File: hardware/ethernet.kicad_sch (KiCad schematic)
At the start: 32 parts, among them J2 DGUK411Q211DB2A1DP2, U2 W5500, X2 25MHz

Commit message: hardware: 4-layer board, placement on both sides, J1 dimensioned
Takes the PCB from bare footprints to a fully placed 4-layer board. No
copper is routed yet and no zones are poured.

Stackup and outline
  Two inner copper layers added: In1.Cu intended as a solid ground plane
  directly beneath the component side, In2.Cu for power distribution. The
  board stays 62 x 68 mm. It is deliberately NOT grown: depth adds mass and
  lengthens the moment arm from the RJ45 cable back to the GPIB connector,
  and the mechanical load path is the connector's two M3 jackscrews on
  46.8 mm centres rather than its 24 signal contacts.

Placement
  All 90 footprints placed: 19 on F.Cu, 71 on B.Cu. Assembly is by hand, so
  back-side passives cost nothing and the 3D-printed enclosure accommodates
  them. Each decoupling capacitor sits on B.Cu directly beneath its IC's
  supply pin, so the connection is a through-via rather than a trace - the
  tightest supply loop available, and it costs no front-side area. That is
  what let the board stay 62 x 68 at ~35% front-side courtyard utilisation
  instead of the 68.7% a single-sided layout needed.

  Verified: zero courtyard overlaps; crystal load caps 0.00-4.00 mm from
  their crystals; C_U3a1 and C_U4a1 at 0.00 mm from their transceivers.

  Done with KiCad's own Flip() transform via the pcbnew Python API, one
  atomic pass, so pads, silkscreen, courtyards and 3D model offsets all
  moved correctly. auto_place_from_schematic was tried and rejected: it
  scored 15 -> 0, planned two parts to identical coordinates and put one
  off-board.

J1 GPIB connector
  Rotated 180 so the pad rows sit at the front edge and the shroud
  overhangs off-board, instead of the body consuming 24 mm of board depth.
  Set back so the two M3 mounting holes are 10.70 mm from the front edge
  per the mechanical drawing; hole span measures 46.80 mm, matching the
  datasheet. This costs 7.84 mm of board depth versus the earlier position
  and reduces the overhang to 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
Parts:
- C_1V2O1, C_BIAS1, C_ETHa1, C_ETHb1, C_ETHbulk1, C_ETHc1, C_ETHd1, C_RCT1, C_TCT1, C_TOCAP1, C_VDD1, C_X2a1, C_X2b1: footprint (none) -> Capacitor_SMD:C_0805_2012Metric
- L2: footprint (none) -> Inductor_SMD:L_0603_1608Metric
- RSET1, R_B1, R_INTP1, R_LEDL1, R_LEDR1, R_RSTP1, R_RX1, R_RX2, R_T1, R_T2, R_T3, R_T4, R_TX1, R_TX2, R_XF1: footprint (none) -> Resistor_SMD:R_0805_2012Metric
- X2: footprint (none) -> Crystal:Crystal_SMD_3225-4Pin_3.2x2.5mm
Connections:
- net GND: now also J2.S1, J2.S2

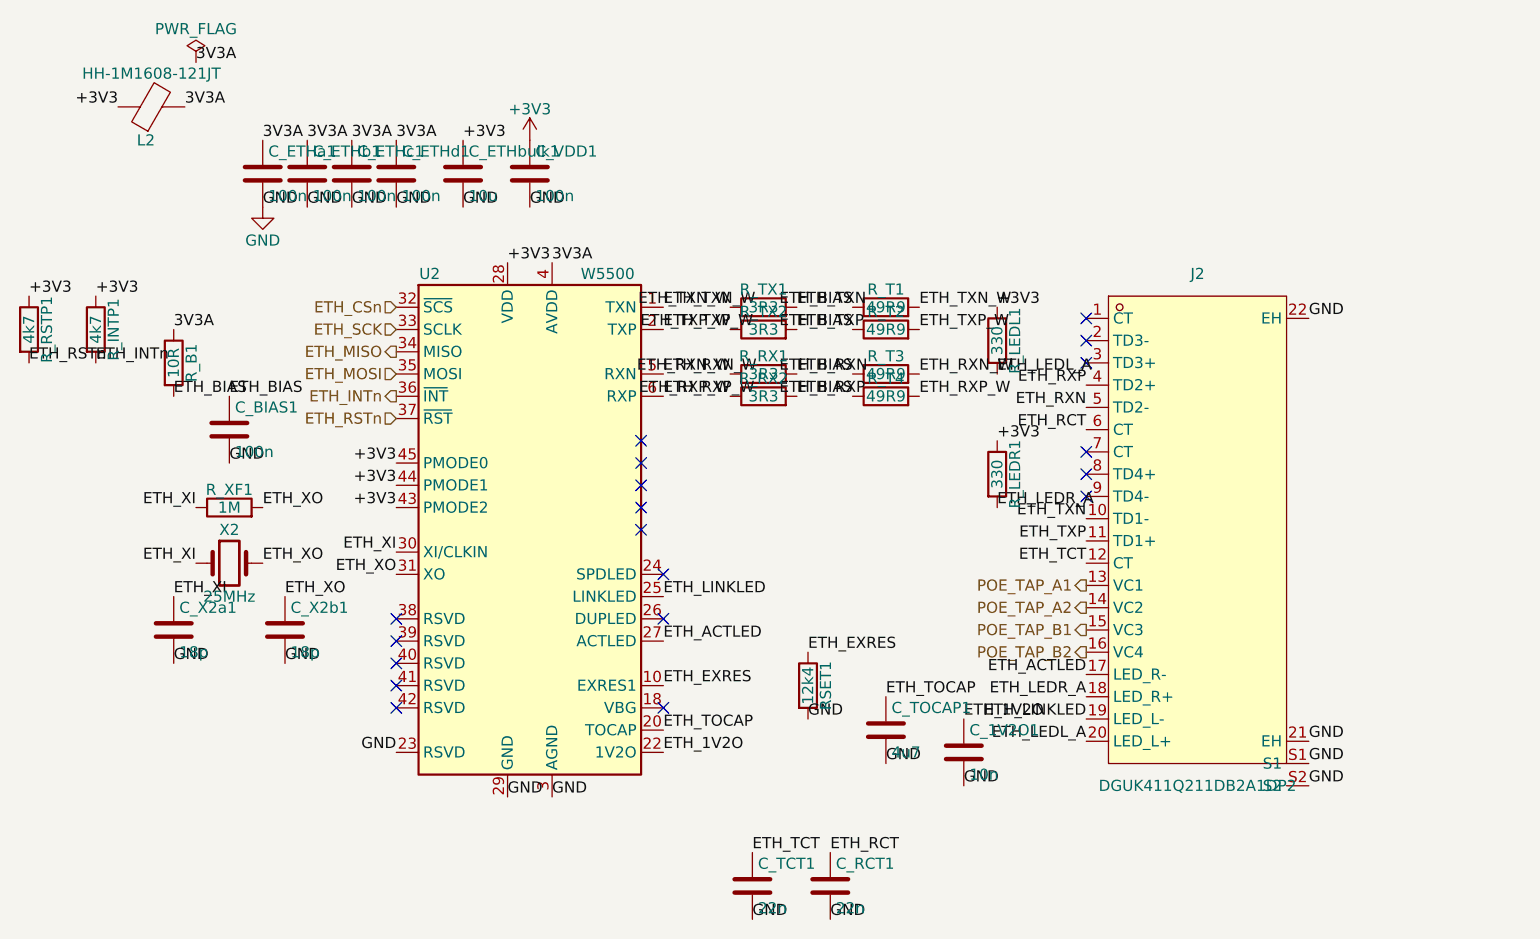
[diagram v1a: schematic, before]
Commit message: hardware: USB-C alternate power source, J2 swapped to HanRun HR871150C
Implements the USB-C-as-alternative-power-source design (design-spec
§30.1): a 1x3 2.54mm header (J4) selects the system rail source via a
jumper rather than a diode-OR, since a Schottky drop would put +5V_SYS
below the SN75160B/161B's 4.75V minimum. Pin 1 = +5V_POE (M1's isolated
output), pin 2 = +5V_SYS (everything downstream), pin 3 = VBUS (from
J3's USB-C pads, already present with 5k1 CC pull-downs). R_G1/C_G1 stay
referenced to +5V_SYS along with Q1's source (R-HW-020): the gate
pull-up must track whichever rail the source actually sits on, or Q1
turns on with IOVDD absent whenever the other source is unpowered.

J2 (PoE RJ45) swapped from a generic MagJack footprint to the actual
ordered part, HanRun HR871150C (LCSC C19724786), correcting the PoE tap
pin numbers (J2.7-10, was J2.13-16) and the shield/ground pin scheme
against its real datasheet pinout.

Added docs/rp2354a-pinmap.md (RP2354A pin assignments) and
hardware/adapter.kicad_dru (project DRC rules). netlist-check.py's
bias-rail-discipline check extended to also flag +5V_SYS, matching the
new rail.
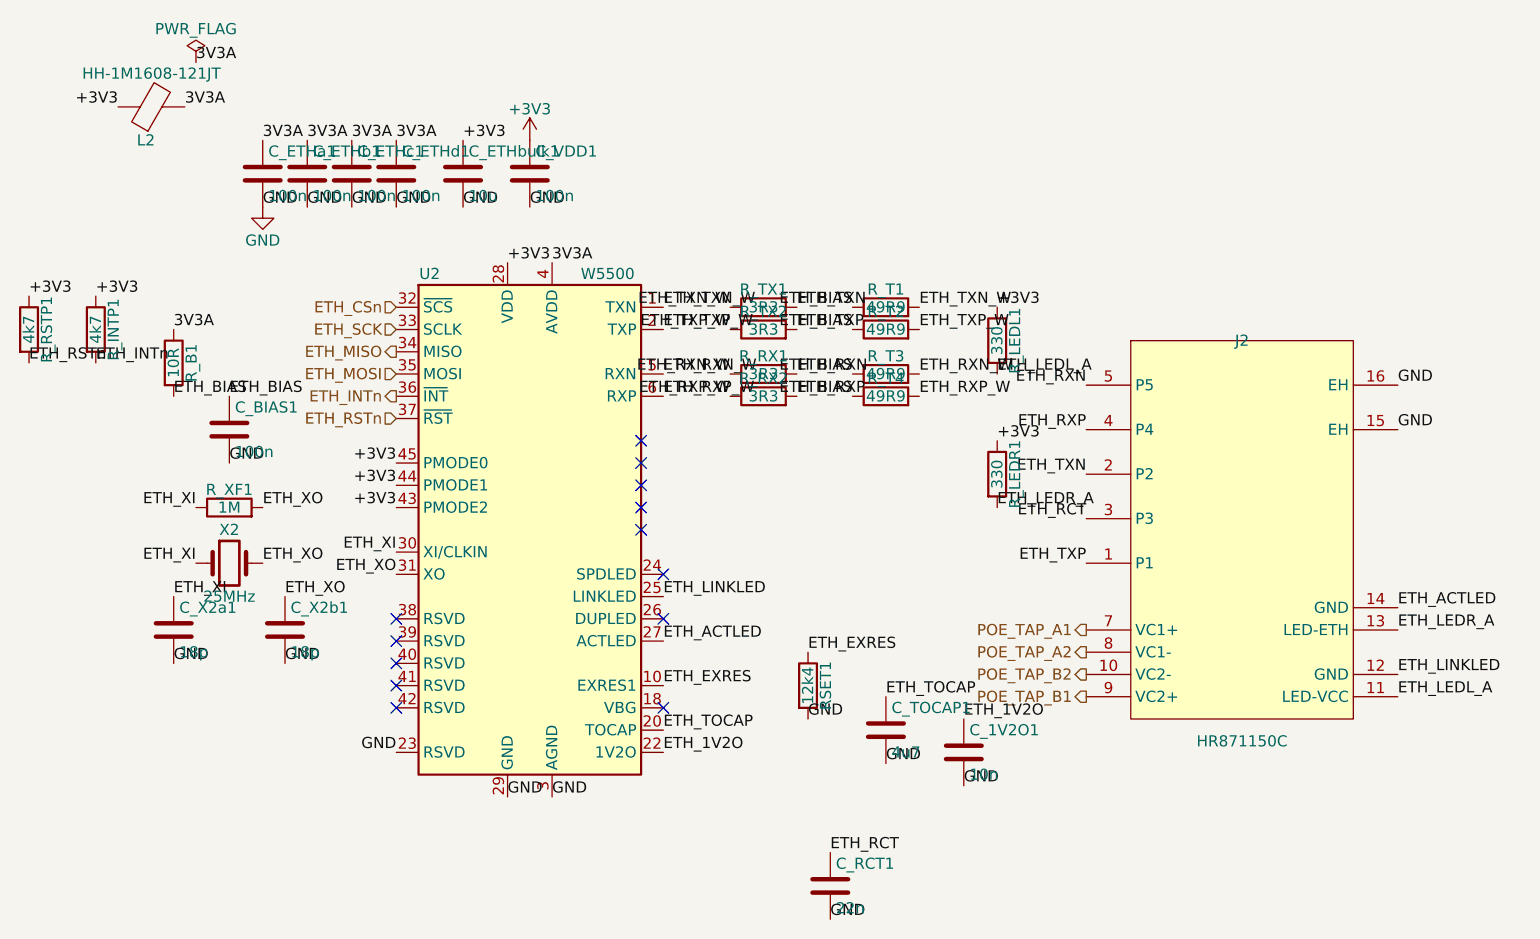
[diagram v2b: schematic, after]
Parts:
- removed C_TCT1: 22n, Capacitor_SMD:C_0805_2012Metric, symbol Device:C
- removed J2: DGUK411Q211DB2A1DP2, adapter:RJ45-TH_DGUK411Q211DB2A1DP2, symbol adapter:DGUK411Q211DB2A1DP2
- added J2: HR871150C, adapter:RJ45-TH_HR871150C, symbol hr871150:HR871150C
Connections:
- net ETH_ACTLED: now also J2.14 (GND)
- net ETH_LEDL_A: now also J2.11 (LED-VCC)
- net ETH_LEDR_A: now also J2.13 (LED-ETH)
- net ETH_LINKLED: now also J2.12 (GND)
- net ETH_RCT: now also J2.3 (P3)
- net ETH_RXN: now also J2.5 (P5)
- net ETH_RXP: now also J2.4 (P4)
- net ETH_TXN: now also J2.2 (P2)
- net ETH_TXP: now also J2.1 (P1)
- net GND: now also J2.15 (EH), J2.16 (EH)
- net POE_TAP_A1: now also J2.7 (VC1+)
- net POE_TAP_A2: now also J2.8 (VC1-)
- net POE_TAP_B1: now also J2.9 (VC2+)
- net POE_TAP_B2: now also J2.10 (VC2-)
- no-connect marks 19 -> 13
